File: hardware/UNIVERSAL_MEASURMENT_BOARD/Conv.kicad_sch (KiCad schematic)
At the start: 99 parts, among them U10 L7805ABD2T-TR, U11 L7812ABD2T-TR, U12 L78L15ACD13TR, U13 L79L15ACD13TR, U14 ISL21010CFH315Z-TK, U15 ISL21010CFH330Z-TK, U5 TPS54202HDDCR, U6 TPS54202HDDCR, U7 LT3471EDD#PBF, U8 UA78M33CDCYRG3, U9 UA78M33CDCYRG3

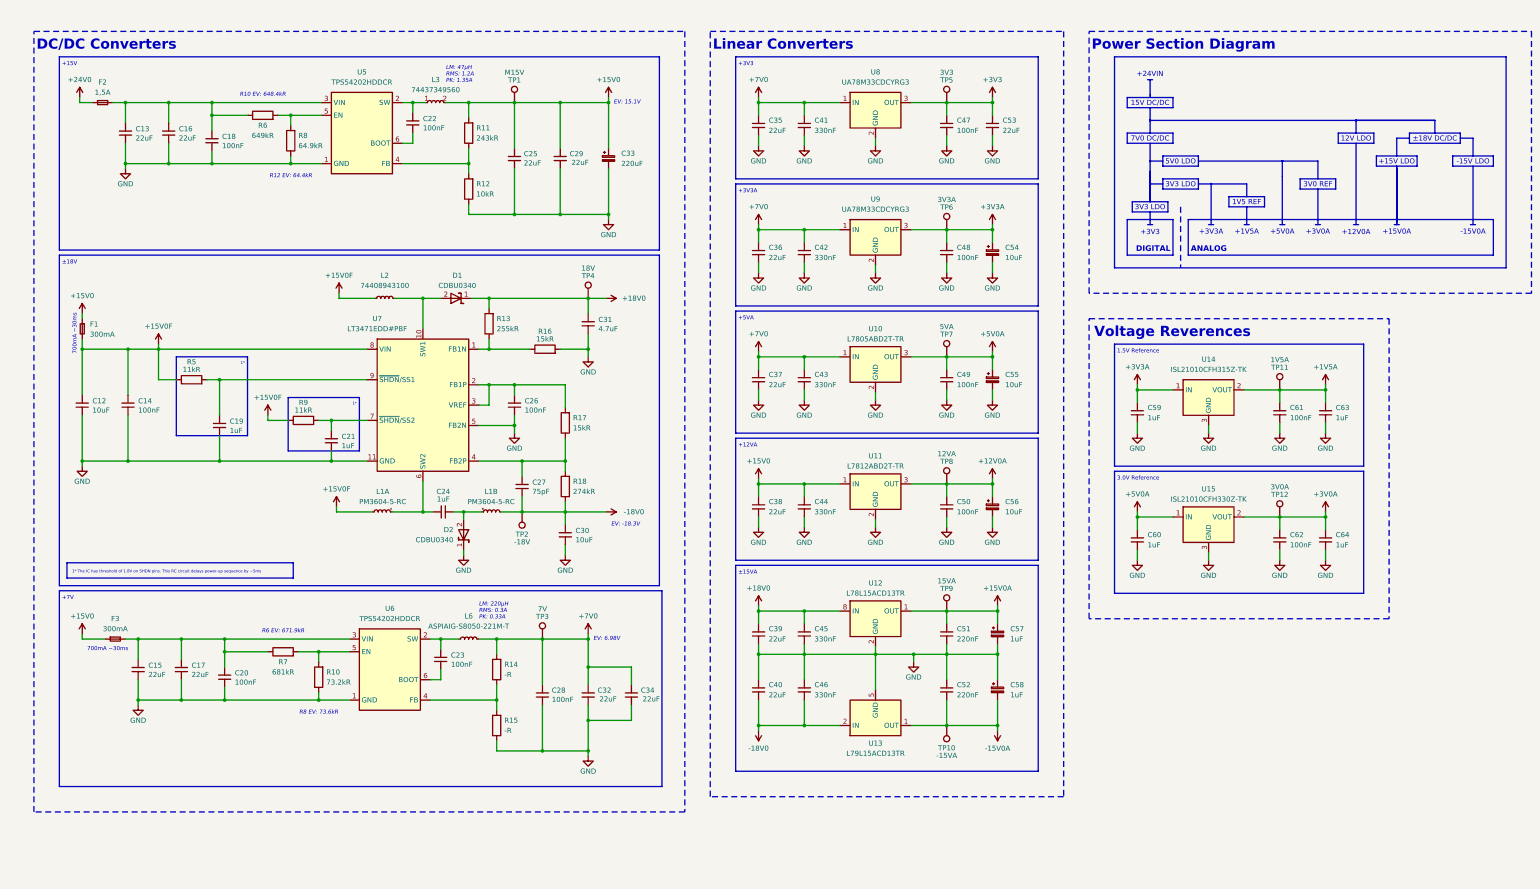
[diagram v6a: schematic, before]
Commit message: solved DRC problems
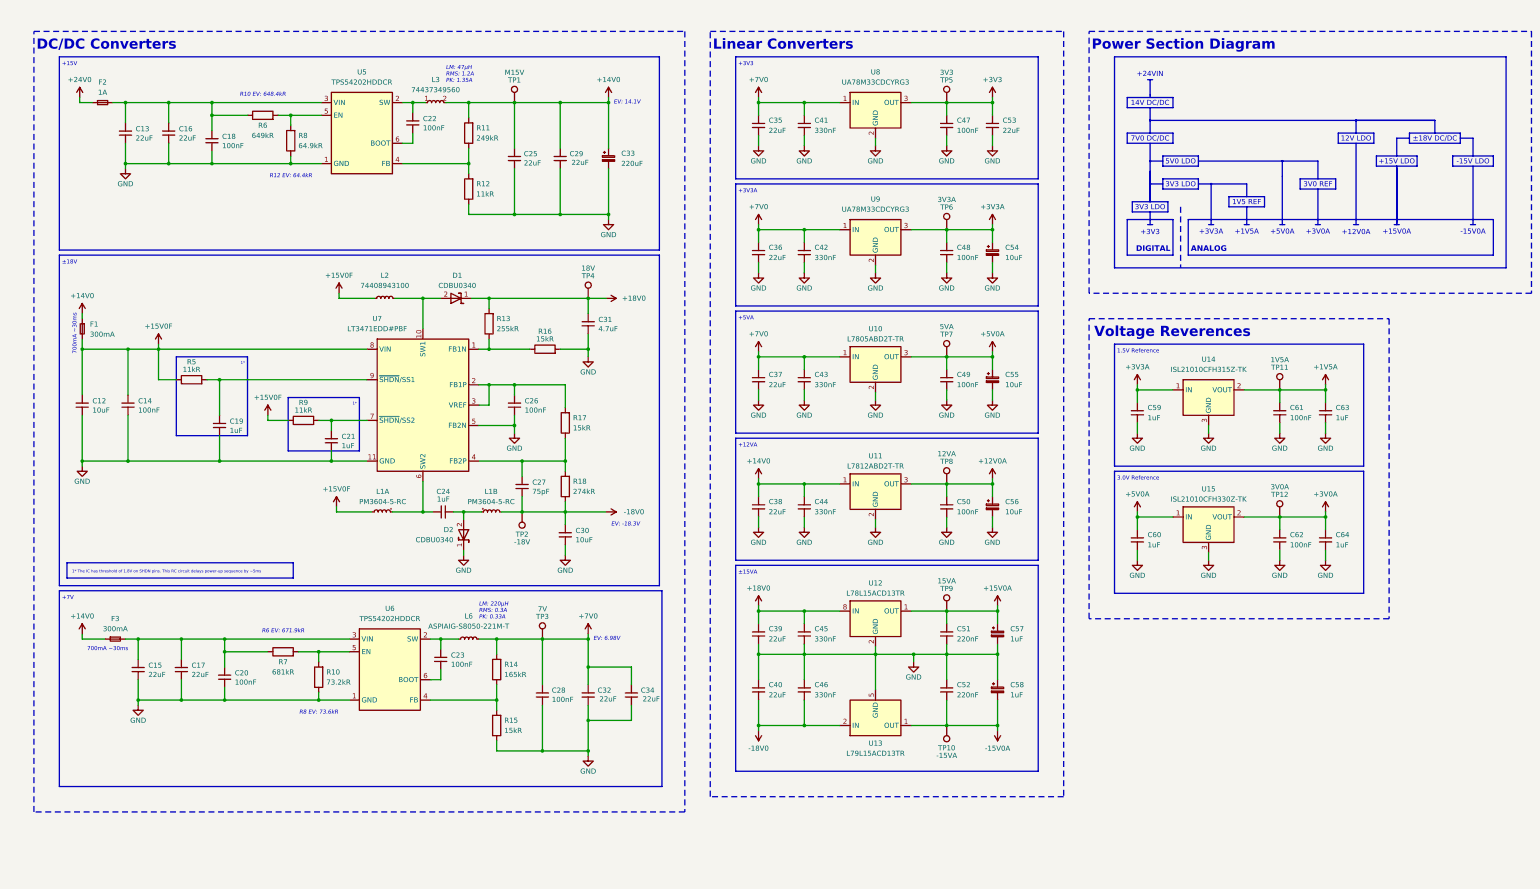
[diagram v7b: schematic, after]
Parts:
- F2: value 1,5A -> 1A
- R11: value 243kR -> 249kR
- R12: value 10kR -> 11kR
- R14: value -R -> 165kR
- R15: value -R -> 15kR
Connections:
- net +15V0 renamed +14V0
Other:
- note added: "14V DC/DC"
- note added: "EV: 14.1V"
- note removed: "15V DC/DC"
- note removed: "EV: 15.1V"
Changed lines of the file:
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@@
 	(title_block
 		(title "Universal Measurment Board")
-		(date "2026-02-02")
-		(rev "1.7.15")
+		(date "2026-03-26")
+		(rev "1.9.21")
 		(company "PUT Motorsport Formula Student Team")
 		(comment 1 "Designed by Marcin Trzmiel under")
@@
 		)
 	)
-	(text "EV: 15.1V"
+	(text "EV: 14.1V"
 		(exclude_from_sim no)
 		(at 168.275 40.64 0)
@@
 		)
 	)
-	(text "15V DC/DC\n\n"
+	(text "14V DC/DC\n\n"
 		(exclude_from_sim no)
 		(at 302.26 41.91 0)
@@
 			)
 		)
-		(property "Value" "+15V0"
+		(property "Value" "+14V0"
 			(at 35.56 168.91 0)
 			(show_name no)
@@
 			)
 		)
-		(property "Value" "1,5A"
+		(property "Value" "1A"
 			(at 40.64 38.1 0)
 			(show_name no)
@@
 			)
 		)
-		(property "Value" "+15V0"
+		(property "Value" "+14V0"
 			(at 167.005 34.925 0)
 			(show_name no)
@@
 			)
 		)
-		(property "Value" "243kR"
+		(property "Value" "249kR"
 			(at 133.985 49.53 0)
 			(show_name no)
@@
 	)
 	(symbol
-		(lib_name "L78L15ACD13TR_1")
 		(lib_id "L78L15ACD13TR:L78L15ACD13TR")
 		(at 233.68 168.91 0)
@@
 			)
 		)
-		(property "Value" "-R"
+		(property "Value" "15kR"
 			(at 140.97 197.485 0)
 			(show_name no)
@@
 			)
 		)
-		(property "Value" "+15V0"
+		(property "Value" "+14V0"
 			(at 204.47 130.175 0)
 			(show_name no)
@@
 			)
 		)
-		(property "Value" "10kR"
+		(property "Value" "11kR"
 			(at 133.985 63.5 0)
 			(show_name no)
@@
 			)
 		)
-		(property "Value" "+15V0"
+		(property "Value" "+14V0"
 			(at 35.56 88.9 0)
 			(show_name no)
@@
 			)
 		)
-		(property "Value" "-R"
+		(property "Value" "165kR"
 			(at 140.97 183.515 0)
 			(show_name no)
